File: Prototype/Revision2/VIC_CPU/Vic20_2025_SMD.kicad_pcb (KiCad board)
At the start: 2 copper layers, 99.1 x 99.1 mm, 140 parts, among them J1 +5V, J2 BOOT SEL, J21 PROGRAM, J3 SWD, J4 USB_B_Micro, J5 VGA, J6 Vic20 Cartridge Connector, J7 I/O Board Connector, J8 Audio / Video, J9 Frame Buffer, U1 W25Q16JVSSIQ, U10 IS6xC1024AL-xxH, U11 6502 CPU, U12 74CBTD3861, U13 74LVC245A, U14 74LVC245A, U15 W25Q16JVSSIQ, U16 MIC5504-1.2YM5, U17 LD1117S33TR_SOT223, U2 TLV74311PDBVR, U3 RP2350B-QFN80, U4 iCE40HX4K-TQ144, U5 74CBTD3861, U6 6561 VIC, U7 74CBTD3861, U8 74CBTD3861, U9 74CBTD3861, Y1 12MHz

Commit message: - As the prototype currently spans 4 boards I have decided to spin a prototype revision 2 (two board prototype set) before i commit to the final layout and design.
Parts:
- removed C1: 100nf, Capacitor_SMD:C_0603_1608Metric
- removed R1: 10k, Resistor_SMD:R_0603_1608Metric
- removed U1: W25Q16JVSSIQ, Package_SO:SOIC-8_5.3x5.3mm_P1.27mm
- added C51: 100nf, Capacitor_SMD:C_0603_1608Metric, F.Cu at (142.6, 99.0)
- added C52: 4.7uf, Capacitor_SMD:C_0603_1608Metric, F.Cu at (142.6, 101.5)
- added J10: DM3D-SF, _Custom:DM3DSF_SDCard, F.Cu at (114.6, 78.0)
- added R41: 10k, Resistor_SMD:R_0603_1608Metric, F.Cu at (142.6, 104.0)
- added R42: 10k, Resistor_SMD:R_0603_1608Metric, F.Cu at (142.6, 106.5)
- added R43: 10k, Resistor_SMD:R_0603_1608Metric, F.Cu at (142.6, 109.0)
- added R44: 10k, Resistor_SMD:R_0603_1608Metric, F.Cu at (142.6, 111.5)
- added R45: 10k, Resistor_SMD:R_0603_1608Metric, F.Cu at (142.6, 114.0)
- added R46: 10k, Resistor_SMD:R_0603_1608Metric, F.Cu at (142.6, 116.5)
- added R47: 10k, Resistor_SMD:R_0603_1608Metric, F.Cu at (142.6, 119.0)
- J4: footprint Dave Footprints:USB_Micro-B_Amphenol_10103594-0001LF_Horizontal -> _Custom:USB_Micro-B_Amphenol_10103594-0001LF_Horizontal
- R16: moved to B.Cu
- R2: value 1k -> 2k2
- U3: value RP2350B-QFN80 -> RP2354B-QFN80
- moved R2 33.2 mm to (119.2, 104.3), turned to 0 degrees
- moved C6 17.4 mm to (100.6, 88.3)
- moved U2 17.4 mm to (101.0, 85.6)
- moved C4 17.4 mm to (101.6, 82.9)
- moved J4 9.23 mm to (117.9, 89.6)
- moved R16 3.21 mm to (112.1, 69.8), turned to 180 degrees
- moved R6 0.10 mm to (110.7, 91.5)
- moved R7 0.10 mm to (112.2, 91.5)
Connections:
- U3 pad 70: /Vic20_2025_SMD/2350_QSPI.SD3 -> unconnected-(U3-QSPI_SD3-Pad70)
- U3 pad 71: /Vic20_2025_SMD/2350_QSPI.SCK -> unconnected-(U3-QSPI_SCLK-Pad71)
- U3 pad 72: /Vic20_2025_SMD/2350_QSPI.SD0 -> unconnected-(U3-QSPI_SD0-Pad72)
- U3 pad 73: /Vic20_2025_SMD/2350_QSPI.SD2 -> unconnected-(U3-QSPI_SD2-Pad73)
- U3 pad 74: /Vic20_2025_SMD/2350_QSPI.SD1 -> unconnected-(U3-QSPI_SD1-Pad74)
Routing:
- net /Vic20_2025_SMD/CA6: track 0.00 -> 29.4 mm
- net /Vic20_2025_SMD/CA7: track 0.00 -> 28.4 mm
- net /Vic20_2025_SMD/CA5: track 0.00 -> 27.3 mm
- net /Vic20_2025_SMD/CD1: track 0.00 -> 27.2 mm
- net /Vic20_2025_SMD/CD2: track 0.00 -> 26.6 mm
- net /Vic20_2025_SMD/CD3: track 0.00 -> 26.0 mm
- net /Vic20_2025_SMD/CD4: track 0.00 -> 25.4 mm
- net /Vic20_2025_SMD/CD7: track 0.00 -> 25.2 mm
- net /Vic20_2025_SMD/CA0: track 0.00 -> 25.0 mm
- net /Vic20_2025_SMD/CA4: track 0.00 -> 24.9 mm
- net /Vic20_2025_SMD/CD5: track 0.00 -> 24.8 mm
- net /Vic20_2025_SMD/CD6: track 0.00 -> 24.8 mm
- net /Vic20_2025_SMD/CA3: track 0.00 -> 23.8 mm
- net /Vic20_2025_SMD/CA1: track 0.00 -> 23.6 mm
- net /Vic20_2025_SMD/CA2: track 0.00 -> 23.6 mm
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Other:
- board text added: "Rev A - 16/08/2026 Dave Gaunt"
- board text removed: "Rev B - 17/09/2024 Dave Gaunt"

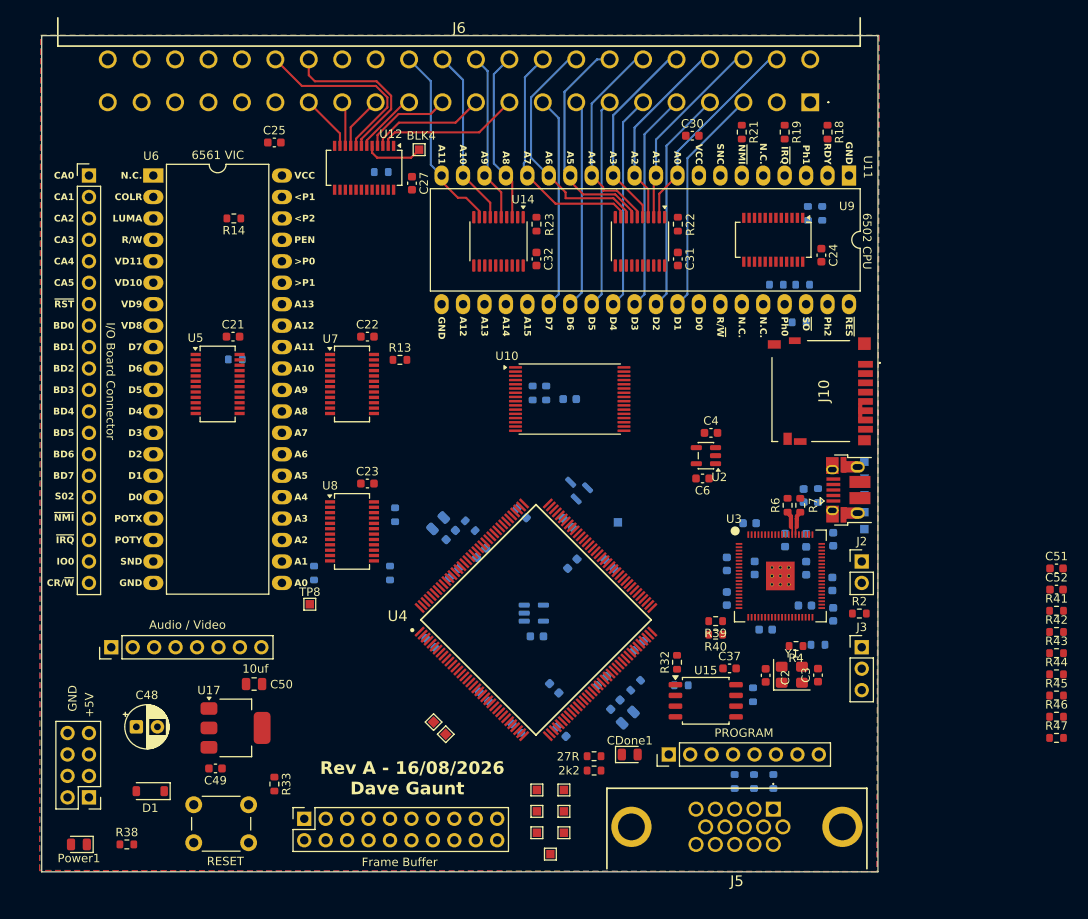
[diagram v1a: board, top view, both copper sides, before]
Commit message: - Initial component placement for protype 2, no routing done yet.
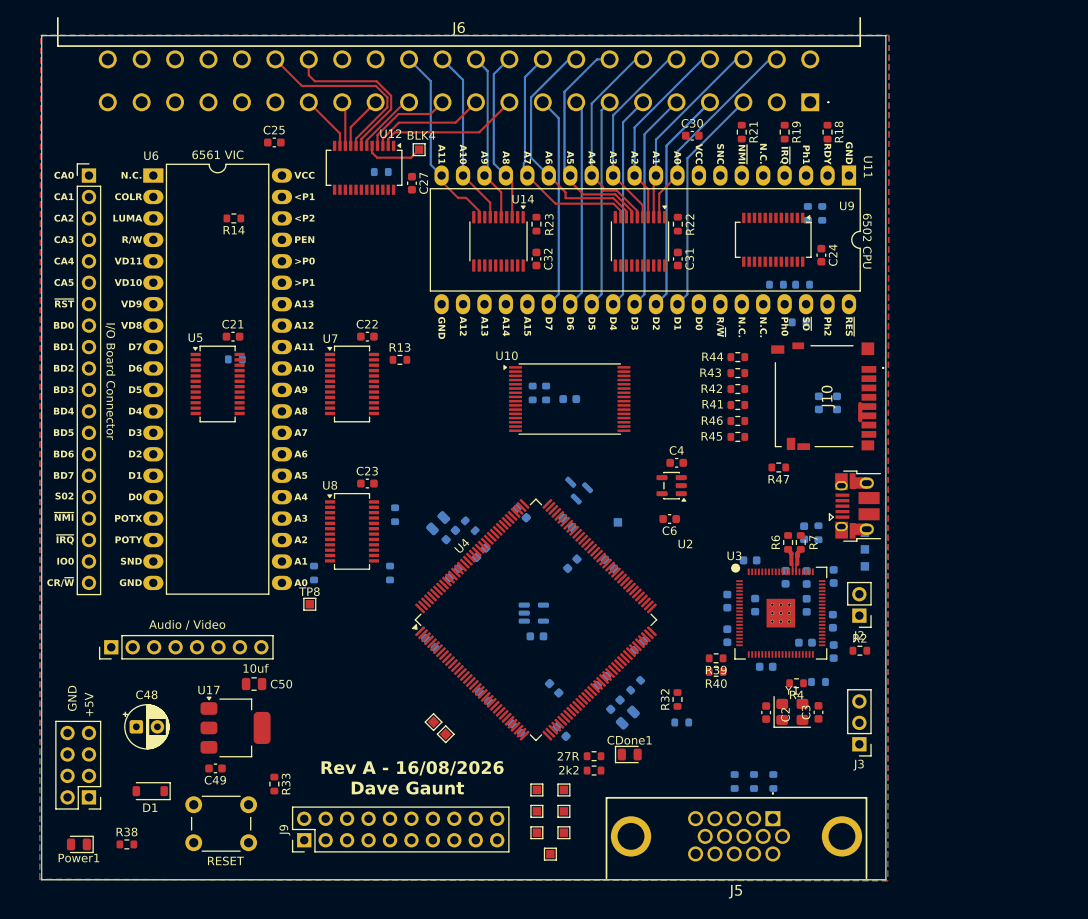
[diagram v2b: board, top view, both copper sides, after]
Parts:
- removed C37: 100nf, Capacitor_SMD:C_0603_1608Metric
- removed J21: PROGRAM, Connector_PinHeader_2.54mm:PinHeader_1x08_P2.54mm_Vertical
- removed R31: 10k, Resistor_SMD:R_0603_1608Metric
- removed U15: W25Q16JVSSIQ, Package_SO:SOIC-8_5.3x5.3mm_P1.27mm
- C51, C52: moved to B.Cu
- J9: footprint Connector_PinSocket_2.54mm:PinSocket_2x10_P2.54mm_Vertical -> Connector_PinHeader_2.54mm:PinHeader_2x10_P2.54mm_Vertical
- U4: footprint SamacSys_Parts:QFP50P2200X2200X160-144N -> Package_QFP:LQFP-144_20x20mm_P0.5mm
- moved R44 53.3 mm to (104.8, 73.9), turned to 180 degrees
- moved R46 51.5 mm to (104.8, 81.5), turned to 180 degrees
- moved R43 50.3 mm to (104.8, 75.8), turned to 180 degrees
- moved R45 48.6 mm to (104.8, 83.4), turned to 180 degrees
- moved R42 47.5 mm to (104.8, 77.7), turned to 180 degrees
- moved R47 45.9 mm to (109.7, 87.0), turned to 180 degrees
- moved R41 44.9 mm to (104.8, 79.6), turned to 180 degrees
- moved C51 34.3 mm to (114.4, 79.3), turned to 90 degrees
- moved C52 34.1 mm to (116.5, 79.3), turned to 90 degrees
- moved J3 11.5 mm to (119.2, 119.8), turned to 180 degrees
- moved J2 6.42 mm to (119.2, 104.5), turned to 180 degrees
- moved C6 6.18 mm to (96.7, 93.1)
- moved U2 5.40 mm to (97.0, 89.2)
- moved C4 5.40 mm to (97.6, 86.5)
- moved C10 4.41 mm to (112.8, 107.8)
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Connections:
- R30 pad 2: Net-(U15-~{CS}) -> iCE40-SS_B
- R32 pad 1: Net-(U15-~{CS}) -> iCE40-SS_B
- R32 pad 2: iCE40-SS_B -> Net-(U4E-IOB_108_SS)
- U3 pad 19: iCE40-SDO -> iCE40-SDI
- U3 pad 20: iCE40-SDI -> iCE40-SDO
- U4 pad 71: iCE40-SS_B -> Net-(U4E-IOB_108_SS)
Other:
- board size 99.1 x 99.1 mm -> 100 x 100 mm
